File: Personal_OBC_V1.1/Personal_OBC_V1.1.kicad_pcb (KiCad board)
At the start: 4 copper layers, 20 x 55 mm, 49 parts, among them IC1 AP2205-33W5-7, J1 PROG PINS, J2 PYRO CHANNELS, J3 POWER IN, J4 USB_B_Micro, J5 636101111001, Q1 SSM6N58NU,LF, SW1 SW_SPDT, U1 STM32F302K8Ux, U2 MS560702BA03-50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

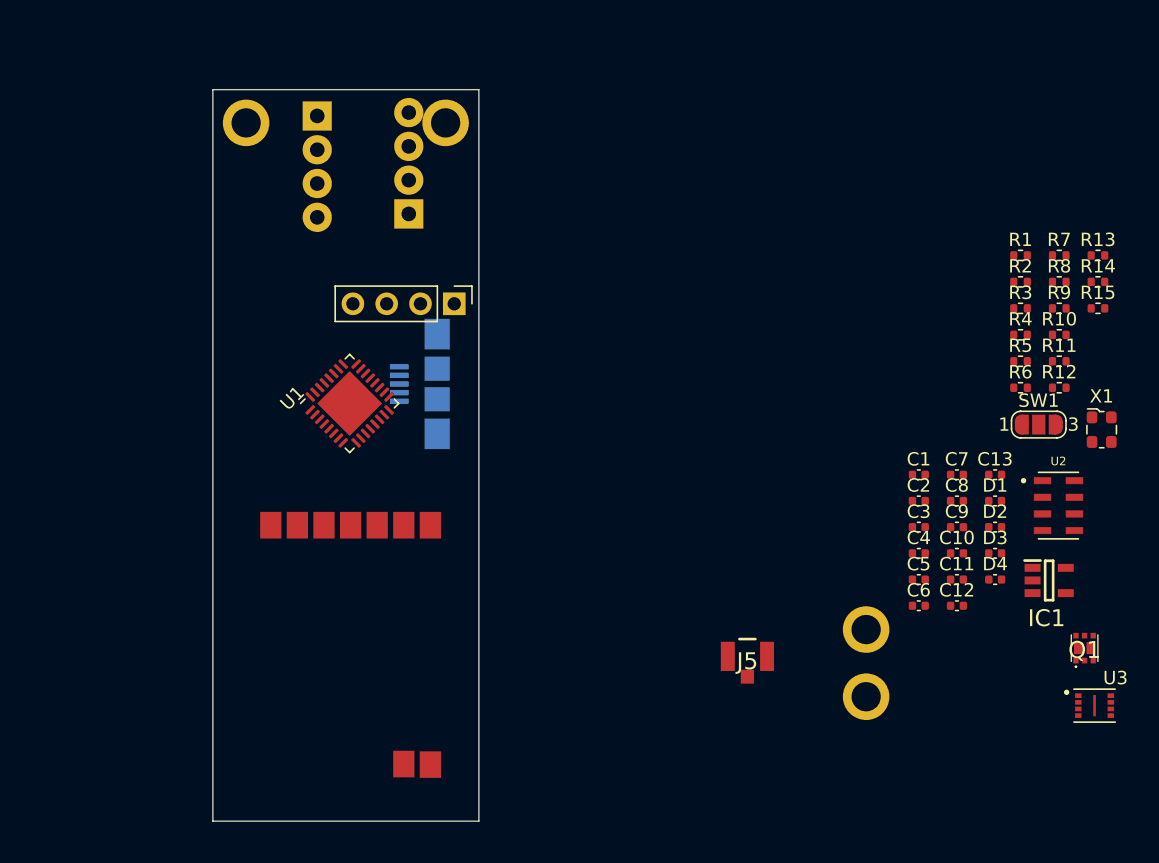
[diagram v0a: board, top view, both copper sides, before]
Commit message: Made deployment board
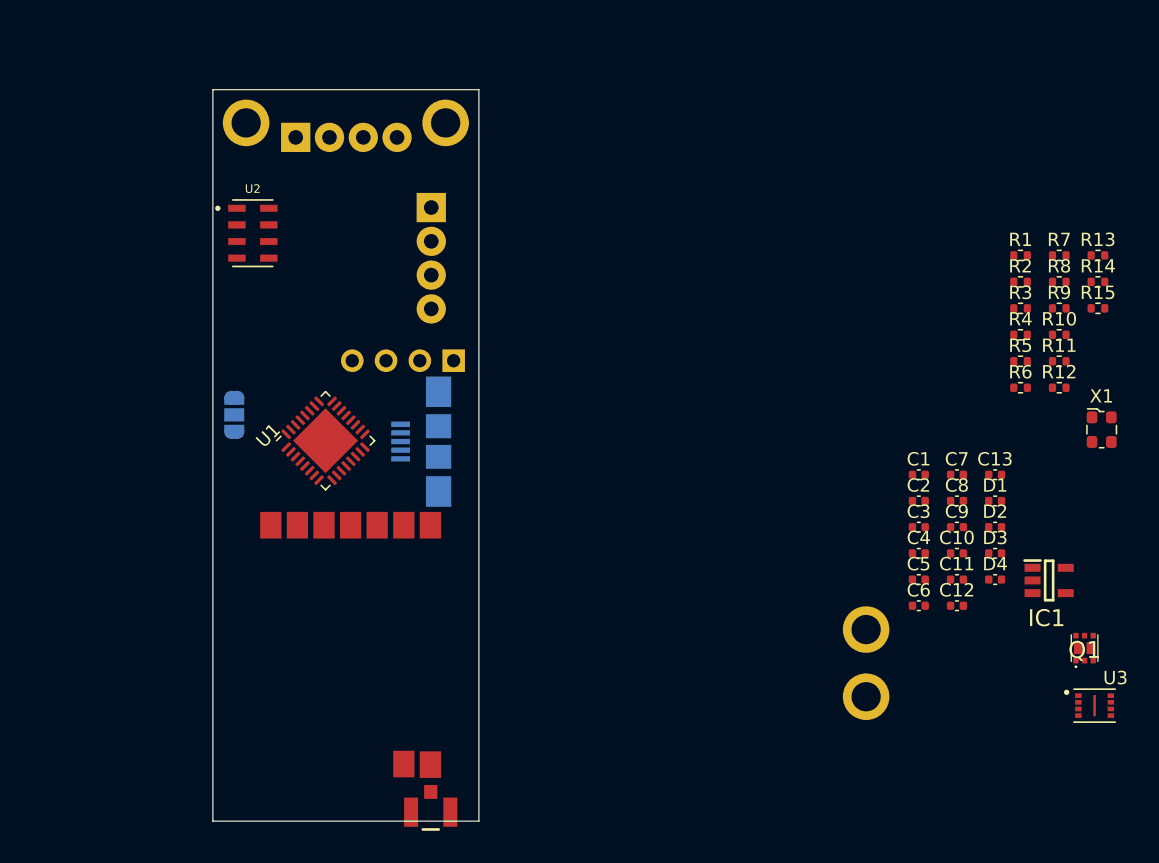
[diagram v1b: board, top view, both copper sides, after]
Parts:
- J1, SW1: moved to B.Cu
- moved U2 63.9 mm to (33.0, 40.8)
- moved SW1 60.5 mm to (31.6, 54.5), turned to -90 degrees
- moved J5 26.5 mm to (46.4, 84.3), turned to 180 degrees
- moved J4 4.33 mm to (45.7, 56.5)
- moved J1 4.28 mm to (48.1, 50.4), turned to 90 degrees
- moved U1 3.34 mm to (38.5, 56.4)
- moved J2 2.28 mm to (36.2, 33.6), turned to 0 degrees
- moved J3 1.76 mm to (46.4, 38.9), turned to -90 degrees

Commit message: Yert
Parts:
- moved Q1 67.5 mm to (37.7, 37.3), turned to -90 degrees
- moved U3 67.1 mm to (35.2, 48.6), turned to -90 degrees
- moved U1 5.07 mm to (34.1, 53.8), turned to 0 degrees
- moved U2 3.63 mm to (33.6, 44.4), turned to 90 degrees
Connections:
- J2 pad 1: PWR+ -> FET_APOGEE
- J2 pad 2: FET_APOGEE -> PWR+
- J2 pad 3: PWR+ -> FET_MAIN
- J2 pad 4: FET_MAIN -> PWR+

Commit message: Yer
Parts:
- moved R10 71.1 mm to (32.0, 83.9)
- moved X1 65.4 mm to (31.5, 53.7)
- moved D2 61.7 mm to (33.1, 36.5)
- moved R7 61.0 mm to (33.1, 35.5), turned to 180 degrees
- moved R12 60.9 mm to (34.2, 39.1), turned to 180 degrees
- moved R9 59.2 mm to (35.2, 36.5), turned to 180 degrees
- moved R11 59.0 mm to (35.8, 38.6), turned to 90 degrees
- moved R6 58.0 mm to (35.2, 35.5), turned to 180 degrees
- moved D3 58.0 mm to (34.1, 83.9), turned to 180 degrees
- moved R14 55.9 mm to (40.9, 38.7), turned to 90 degrees
- moved IC1 55.7 mm to (42.5, 43.0), turned to 180 degrees
- moved R13 54.0 mm to (42.7, 39.2)
- moved C11 53.4 mm to (33.4, 57.0), turned to -90 degrees
- moved R8 52.3 mm to (41.9, 36.7)
- moved C10 52.2 mm to (34.5, 56.3), turned to -90 degrees
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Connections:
- C12 pad 1: PWR+ -> BATT+
- IC1 pad 1: PWR+ -> BATT+
- IC1 pad 3: PWR+ -> BATT+

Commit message: Some personal pcb work
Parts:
- removed IC1: AP2205-33W5-7, AP2205-33W5-7:SOT95P282X130-5N
- removed J4: USB_B_Micro, Connector_USB:USB_Micro-B_Amphenol_10104110_Horizontal
- added U5: AP2205-33W5-7, AP2205-33W5-7:SOT95P282X130-5N, F.Cu at (40.6, 36.7)
- J2: value PYRO CHANNELS -> PROG PINS; footprint TerminalBlock_Phoenix:TerminalBlock_Phoenix_MPT-0,5-4-2.54_1x04_P2.54mm_Horizontal -> Connector_PinHeader_2.54mm:PinHeader_1x04_P2.54mm_Vertical
- J3: value POWER IN -> PROG PINS; footprint TerminalBlock_Phoenix:TerminalBlock_Phoenix_MPT-0,5-4-2.54_1x04_P2.54mm_Horizontal -> Connector_PinHeader_2.54mm:PinHeader_1x04_P2.54mm_Vertical
- moved R1 71.1 mm to (19.6, 43.2), turned to 90 degrees
- moved C1 62.2 mm to (27.2, 31.7)
- moved R15 58.2 mm to (38.4, 49.0)
- moved C2 54.6 mm to (30.9, 44.8)
- moved D4 51.5 mm to (40.5, 48.9), turned to 180 degrees
- moved R2 47.6 mm to (43.8, 36.7), turned to -90 degrees
- moved R3 47.6 mm to (43.8, 38.7), turned to -90 degrees
- moved C9 46.6 mm to (42.0, 47.2), turned to -90 degrees
- moved C7 18.7 mm to (18.0, 43.8)
- moved C8 18.7 mm to (18.0, 42.8)
- moved U1 16.5 mm to (35.3, 39.1), turned to 90 degrees
- moved SW1 16.1 mm to (22.5, 41.2), turned to 180 degrees
- moved D1 15.0 mm to (30.5, 30.0), turned to 0 degrees
- moved R5 14.2 mm to (30.5, 31.0), turned to 180 degrees
- moved R8 11.6 mm to (32.5, 30.0), turned to 180 degrees
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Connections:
- J1 pad 1: SYS_SWDIO -> SYS_SWCLK
- J1 pad 2: SYS_SWCLK -> SYS_SWDIO
- J2 pad 1: FET_APOGEE -> FET_MAIN
- J2 pad 3: FET_MAIN -> FET_APOGEE
- R2 pad 1: PWR+ -> BATT+
- U1 pad 18: SENSE_MAIN -> SENSE_APOGEE
- U1 pad 19: SENSE_APOGEE -> SENSE_MAIN
- U1 pad 2: RCC_OCC_IN -> RCC_OSC_IN
- U1 pad 3: RCC_OCC_OUT -> RCC_OSC_OUT
- U2 pad 1: 3.3V -> +3.3V
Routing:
- net PWR+: track 0.00 -> 14.4 mm
- net GND: track 0.00 -> 13.9 mm, vias 0 -> 14
- net BATT+: track 0.00 -> 12.8 mm
- net SENSE_APOGEE: track 0.00 -> 7.15 mm, vias 0 -> 2
- net FET_MAIN: track 0.00 -> 6.62 mm
- net FET_APOGEE: track 0.00 -> 6.27 mm
- net SENSE_MAIN: track 0.00 -> 6.22 mm, vias 0 -> 2
- net Net-(Q1-G1): track 0.00 -> 2.72 mm, vias 0 -> 2
- net Net-(Q1-G2): track 0.00 -> 2.55 mm
- net +3.3V: track 0.00 -> 2.09 mm, vias 0 -> 4
- net CS_MEM: track 0.00 -> 1.55 mm, vias 0 -> 1
- net FIRE_MAIN: track 0.00 -> 1.10 mm
- net Net-(D2-A): track 0.00 -> 0.98 mm
- net V_BAT: track 0.00 -> 0.98 mm
- net Net-(D1-A): track 0.00 -> 0.96 mm
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- added copper zone on F.Cu, net +3.3V
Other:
- board size 20 x 55 mm -> 22.9 x 50.8 mm

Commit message: created flower pot and worked on personal board
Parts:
- moved R1 11.4 mm to (30.5, 39.9), turned to 180 degrees
- moved SW1 5.42 mm to (27.8, 39.9), turned to -90 degrees
- moved C11 4.52 mm to (36.1, 45.0), turned to 0 degrees
- moved C10 4.02 mm to (36.1, 44.0), turned to 0 degrees
- moved C2 3.65 mm to (34.3, 43.5), turned to 90 degrees
- moved C3 3.20 mm to (32.4, 43.7)
- moved C4 3.20 mm to (32.3, 45.7)
- moved X1 3.15 mm to (30.4, 44.2)
- moved U1 0.66 mm to (34.7, 39.0)
- moved R3 0.35 mm to (43.8, 39.0)
- moved U2 0.27 mm to (28.2, 35.3)
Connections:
- U1 pad 12: FIRE_APOGEE -> unconnected-(U1-PA5-Pad12)
- U1 pad 13: FIRE_MAIN -> unconnected-(U1-PA6-Pad13)
- U1 pad 15: unconnected-(U1-PB0-Pad15) -> FIRE_MAIN
- U1 pad 20: unconnected-(U1-PA10-Pad20) -> FIRE_APOGEE
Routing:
- net GND: track 13.9 -> 23.5 mm, vias 14 -> 24
- net V_BAT: track 0.98 -> 8.31 mm, vias 0 -> 2
- net RCC_OSC_IN: track 0.00 -> 6.41 mm
- net FIRE_APOGEE: track 0.00 -> 5.86 mm
- net RCC_OSC_OUT: track 0.00 -> 5.75 mm
- net +3.3V: track 2.09 -> 7.10 mm, vias 4 -> 9
- net FIRE_MAIN: track 1.10 -> 5.98 mm
- net SENSE_APOGEE: track 7.15 -> 10.5 mm
- net SENSE_MAIN: track 6.22 -> 9.53 mm
- net Net-(SW1-B): track 0.00 -> 2.70 mm, vias 0 -> 1
- net Net-(U1-NRST): track 0.00 -> 1.66 mm
- net Net-(Q1-G1): track 2.72 -> 4.28 mm
- net BOOT0: track 0.00 -> 1.33 mm
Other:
- board text added: "+"
- board text added: "-"
- board text added: "APO"
- board text added: "MAIN"
- board text added: "SWITCH"

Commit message: Yart
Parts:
- moved R1 2.92 mm to (27.6, 40.0)
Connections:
- U1 pad 25: CS_ALT -> CS_MEM
- U1 pad 29: CS_MEM -> CS_ALT
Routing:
- net CS_ALT: track 0.00 -> 7.31 mm
- net MOSI: track 0.00 -> 7.00 mm, vias 0 -> 2
- net SCLK: track 0.00 -> 6.03 mm
- net MISO: track 0.86 -> 5.01 mm
- net Net-(SW1-B): track 2.70 -> 0.00 mm, vias 1 -> 0
- net BOOT0: track 1.33 -> 0.00 mm
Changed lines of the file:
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@@
       (net 12 "SYS_SWCLK") (pinfunction "PA14") (pintype "bidirectional"))
     (pad "25" smd roundrect (at 1.75 -2.4375 90) (size 0.25 0.875) (layers "F.Cu" "F.Paste" "F.Mask") (roundrect_rratio 0.25)
-      (net 35 "CS_ALT") (pinfunction "PA15") (pintype "bidirectional"))
+      (net 39 "CS_MEM") (pinfunction "PA15") (pintype "bidirectional"))
     (pad "26" smd roundrect (at 1.25 -2.4375 90) (size 0.25 0.875) (layers "F.Cu" "F.Paste" "F.Mask") (roundrect_rratio 0.25)
       (net 36 "SCLK") (pinfunction "PB3") (pintype "bidirectional"))
@@
       (net 38 "MOSI") (pinfunction "PB5") (pintype "bidirectional"))
     (pad "29" smd roundrect (at -0.25 -2.4375 90) (size 0.25 0.875) (layers "F.Cu" "F.Paste" "F.Mask") (roundrect_rratio 0.25)
-      (net 39 "CS_MEM") (pinfunction "PB6") (pintype "bidirectional"))
+      (net 35 "CS_ALT") (pinfunction "PB6") (pintype "bidirectional"))
     (pad "30" smd roundrect (at -0.75 -2.4375 90) (size 0.25 0.875) (layers "F.Cu" "F.Paste" "F.Mask") (roundrect_rratio 0.25)
       (net 40 "unconnected-(U1-PB7-Pad30)") (pinfunction "PB7") (pintype "bidirectional"))
@@
   )
   (footprint "Resistor_SMD:R_0402_1005Metric" (layer "F.Cu")
-    (at 30.53 39.88 180)
+    (at 27.61 40 180)
     (descr "Resistor SMD 0402 (1005 Metric), square (rectangular) end terminal, IPC_7351 nominal, (Body size source: IPC-SM-782 page 72, https://www.pcb-3d.com/wordpress/wp-content/uploads/ipc-sm-782a_amendment_1_and_2.pdf), generated with kicad-footprint-generator")
     (tags "resistor")
@@
   (segment (start 30.7 44.35) (end 32.135002 44.35) (width 0.3) (layer "F.Cu") (net 3))
   (segment (start 33.6 42.717106) (end 33.6 43.982501) (width 0.3) (layer "F.Cu") (net 4))
+  (segment (start 33.91 41.415) (end 33.91 42.407106) (width 0.3) (layer "F.Cu") (net 4))
+  (segment (start 33.91 42.407106) (end 33.6 42.717106) (width 0.3) (layer "F.Cu") (net 4))
   (segment (start 32.347501 45.235) (end 31.185 45.235) (width 0.3) (layer "F.Cu") (net 4))
   (segment (start 31.185 45.235) (end 31.1 45.15) (width 0.3) (layer "F.Cu") (net 4))
-  (segment (start 33.91 42.407106) (end 33.6 42.717106) (width 0.3) (layer "F.Cu") (net 4))
   (segment (start 33.6 43.982501) (end 32.347501 45.235) (width 0.3) (layer "F.Cu") (net 4))
-  (segment (start 33.91 41.415) (end 33.91 42.407106) (width 0.3) (layer "F.Cu") (net 4))
   (segment (start 35.1695 42.886535) (end 35.1695 43.04) (width 0.3) (layer "F.Cu") (net 5))
   (segment (start 26.07 33.45) (end 26.03 33.49) (width 0.5) (layer "F.Cu") (net 5))
@@
   (segment (start 37.1585 31) (end 37.96 31.8015) (width 0.3) (layer "F.Cu") (net 21))
   (segment (start 37.96 31.8015) (end 37.96 32.71) (width 0.3) (layer "F.Cu") (net 21))
-  (segment (start 31.3875 40.2275) (end 32.2225 40.2275) (width 0.3) (layer "F.Cu") (net 22))
-  (segment (start 31.04 39.88) (end 31.3875 40.2275) (width 0.3) (layer "F.Cu") (net 22))
-  (segment (start 29.22 39.9) (end 29.24 39.88) (width 0.3) (layer "F.Cu") (net 23))
-  (segment (start 29.24 39.88) (end 30.02 39.88) (width 0.3) (layer "F.Cu") (net 23))
-  (via (at 29.22 39.9) (size 0.7) (drill 0.3) (layers "F.Cu" "B.Cu") (net 23))
-  (segment (start 27.77 39.91) (end 27.79 39.89) (width 0.3) (layer "B.Cu") (net 23))
-  (segment (start 27.79 39.89) (end 28.2 39.89) (width 0.3) (layer "B.Cu") (net 23))
-  (segment (start 29.22 39.9) (end 27.78 39.9) (width 0.3) (layer "B.Cu") (net 23))
-  (segment (start 27.78 39.9) (end 27.77 39.91) (width 0.3) (layer "B.Cu") (net 23))
   (segment (start 43.8 37.86) (end 43.79 37.85) (width 0.5) (layer "F.Cu") (net 24))
   (segment (start 43.79 37.85) (end 43.8 37.84) (width 0.5) (layer "F.Cu") (net 24))
@@
   (segment (start 37.618363 37.7275) (end 38.05 37.295863) (width 0.3) (layer "F.Cu") (net 28))
   (segment (start 37.0975 37.7275) (end 37.618363 37.7275) (width 0.3) (layer "F.Cu") (net 28))
+  (segment (start 29.44 38.57) (end 29.44 37.2) (width 0.3) (layer "F.Cu") (net 35))
+  (segment (start 27.62 37.78) (end 28.86 37.78) (width 0.3) (layer "F.Cu") (net 35))
+  (segment (start 28.86 37.78) (end 29.44 37.2) (width 0.3) (layer "F.Cu") (net 35))
+  (segment (start 27.04 37.2) (end 27.62 37.78) (width 0.3) (layer "F.Cu") (net 35))
+  (segment (start 32.2225 39.2275) (end 30.0975 39.2275) (width 0.3) (layer "F.Cu") (net 35))
+  (segment (start 30.0975 39.2275) (end 29.44 38.57) (width 0.3) (layer "F.Cu") (net 35))
+  (segment (start 31.701637 37.7275) (end 31.36 37.385863) (width 0.3) (layer "F.Cu") (net 36))
+  (segment (start 31.36 37.385863) (end 31.36 34.86) (width 0.3) (layer "F.Cu") (net 36))
+  (segment (start 32.2225 37.7275) (end 31.701637 37.7275) (width 0.3) (layer "F.Cu") (net 36))
+  (segment (start 31.36 34.86) (end 29.95 33.45) (width 0.3) (layer "F.Cu") (net 36))
+  (segment (start 29.95 33.45) (end 29.44 33.45) (width 0.3) (layer "F.Cu") (net 36))
+  (segment (start 30.6 37.3975) (end 31.43 38.2275) (width 0.3) (layer "F.Cu") (net 37))
+  (segment (start 29.44 35.95) (end 29.889631 35.95) (width 0.3) (layer "F.Cu") (net 37))
+  (segment (start 29.889631 35.95) (end 30.6 36.660369) (width 0.3) (layer "F.Cu") (net 37))
   (segment (start 41.19 41.379705) (end 41.379819 41.189886) (width 0.25) (layer "F.Cu") (net 37))
   (segment (start 41.19 41.9675) (end 41.19 41.379705) (width 0.25) (layer "F.Cu") (net 37))
+  (segment (start 31.43 38.2275) (end 32.2225 38.2275) (width 0.3) (layer "F.Cu") (net 37))
+  (segment (start 30.6 36.660369) (end 30.6 37.3975) (width 0.3) (layer "F.Cu") (net 37))
   (via (at 41.379819 41.189886) (size 0.7) (drill 0.3) (layers "F.Cu" "B.Cu") (net 37))
+  (segment (start 30.1395 38.23) (end 30.637 38.7275) (width 0.3) (layer "F.Cu") (net 38))
+  (segment (start 30.637 38.7275) (end 32.2225 38.7275) (width 0.3) (layer "F.Cu") (net 38))
+  (segment (start 30.66 35.24) (end 30.12 34.7) (width 0.3) (layer "F.Cu") (net 38))
+  (segment (start 30.12 34.7) (end 29.44 34.7) (width 0.3) (layer "F.Cu") (net 38))
+  (via (at 30.66 35.24) (size 0.7) (drill 0.3) (layers "F.Cu" "B.Cu") (net 38))
+  (via (at 30.1395 38.23) (size 0.7) (drill 0.3) (layers "F.Cu" "B.Cu") (net 38))
+  (segment (start 30.73 35.31) (end 30.66 35.24) (width 0.3) (layer "B.Cu") (net 38))
+  (segment (start 30.73 37.6395) (end 30.73 35.31) (width 0.3) (layer "B.Cu") (net 38))
+  (segment (start 30.1395 38.23) (end 30.73 37.6395) (width 0.3) (layer "B.Cu") (net 38))
   (segment (start 42.0825 41.9675) (end 41.69 41.9675) (width 0.25) (layer "F.Cu") (net 39))
   (segment (start 42.39 41.66) (end 42.0825 41.9675) (width 0.25) (layer "F.Cu") (net 39))

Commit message: Perosnal work
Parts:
- J1: value PROG PINS -> Conn_01x02_Pin; footprint Connector_PinHeader_2.54mm:PinHeader_1x04_P2.54mm_Vertical -> Connector_PinHeader_2.54mm:PinHeader_1x02_P2.54mm_Vertical
- moved J1 0.11 mm to (45.7, 43.9)
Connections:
- J1 pad 1: SYS_SWCLK -> SYS_SWDIO
- J1 pad 2: SYS_SWDIO -> SYS_SWCLK
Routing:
- net SENSE_APOGEE: track 10.5 -> 7.15 mm, vias 2 -> 1
- net SENSE_MAIN: track 9.53 -> 6.22 mm, vias 2 -> 1
- net SYS_SWDIO: track 0.00 -> 1.77 mm, vias 0 -> 1
- net SYS_SWCLK: track 0.00 -> 1.75 mm, vias 0 -> 1
- net CS_MEM: track 1.55 -> 3.17 mm, vias 1 -> 2
- net GND: track 23.5 -> 24.1 mm, vias 24 -> 25
- net SCLK: track 6.03 -> 6.19 mm, vias 0 -> 1
- net MISO: track 5.01 -> 5.11 mm, vias 1 -> 2
